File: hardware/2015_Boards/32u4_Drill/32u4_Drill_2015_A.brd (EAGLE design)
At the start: 31.8 x 55.9 mm, 25 parts, among them U2 XBEE-1B3

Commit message: Update some Capacitor Values
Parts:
- C1, C2, C3, C4: value (none) -> 0.01uF
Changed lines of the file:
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@@
 <?xml version="1.0" encoding="utf-8"?>
 <!DOCTYPE eagle SYSTEM "eagle.dtd">
-<eagle version="6.6.0">
+<eagle version="6.5.0">
 <drawing>
 <settings>
@@
 </element>
 <element name="U$4" library="MRDT-2015-General" package="BTM7752G" value="BTM7752G" x="15.875" y="15.5575"/>
-<element name="C1" library="SparkFun-Passives" package="1206" value="" x="11.1125" y="27.94" rot="R90"/>
-<element name="C2" library="SparkFun-Passives" package="1206" value="" x="20.6375" y="27.94" rot="R90"/>
+<element name="C1" library="SparkFun-Passives" package="1206" value="0.01uF" x="11.1125" y="27.94" rot="R90"/>
+<element name="C2" library="SparkFun-Passives" package="1206" value="0.01uF" x="20.6375" y="27.94" rot="R90"/>
 <element name="R2" library="SparkFun-Passives" package="1206" value="4.7k" x="15.875" y="39.37"/>
 <element name="R4" library="SparkFun-Passives" package="1206" value="4.7k" x="15.875" y="37.1475"/>
@@
 <element name="R6" library="SparkFun-Passives" package="1206" value="1k" x="15.875" y="41.5925"/>
 <element name="R7" library="SparkFun-Passives" package="1206" value="" x="15.875" y="43.815"/>
-<element name="C3" library="SparkFun-Passives" package="1206" value="" x="5.08" y="14.605" rot="R180"/>
-<element name="C4" library="SparkFun-Passives" package="1206" value="" x="5.08" y="12.3825" rot="R180"/>
+<element name="C3" library="SparkFun-Passives" package="1206" value="0.01uF" x="5.08" y="14.605" rot="R180"/>
+<element name="C4" library="SparkFun-Passives" package="1206" value="0.01uF" x="5.08" y="12.3825" rot="R180"/>
 </elements>
 <signals>
@@
 <wire x1="14.475" y1="37.1475" x2="14.1575" y2="37.1475" width="0.4064" layer="1"/>
 <wire x1="8.636" y1="34.29" x2="10.16" y2="34.29" width="0.254" layer="16"/>
+<wire x1="13.0175" y1="37.1475" x2="14.1575" y2="37.1475" width="0.254" layer="16"/>
 <wire x1="10.16" y1="34.29" x2="13.0175" y2="37.1475" width="0.254" layer="16"/>
-<wire x1="13.0175" y1="37.1475" x2="14.1575" y2="37.1475" width="0.254" layer="16"/>
 </signal>
 <signal name="INH">

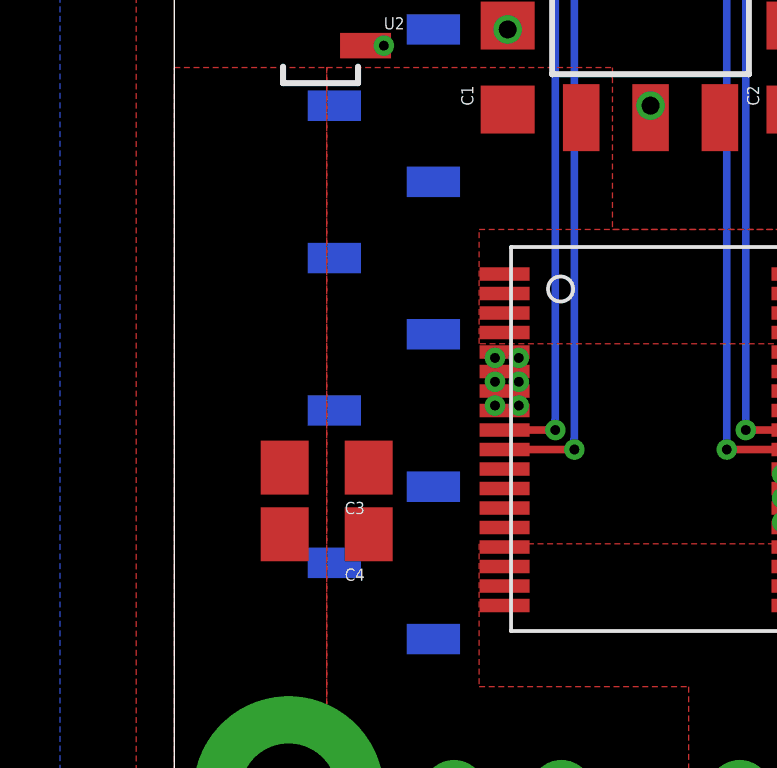
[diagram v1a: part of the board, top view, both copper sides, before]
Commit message: Added a beefy capacitor because the datasheet told me too
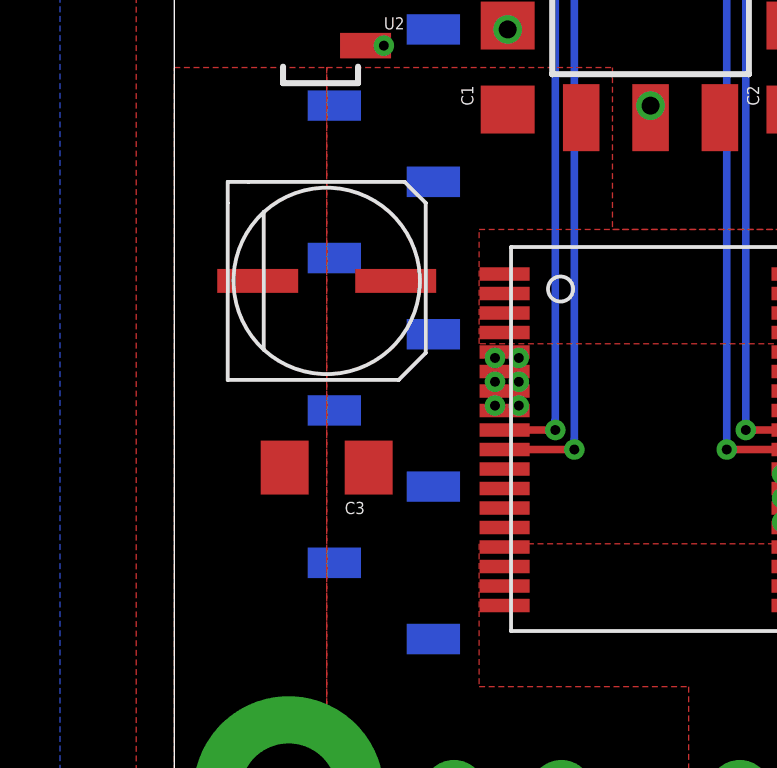
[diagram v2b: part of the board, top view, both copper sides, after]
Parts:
- removed C4: 0.01uF, SparkFun-Passives:1206
- added U$6: 100UF-ELECTRO-CAP, New:ELECTRO-CAP
- C1, C2, C3: value 0.01uF -> 0.1uF
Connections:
- net 12V: now also U$6.POS; no longer C4.1
- net GND: no longer C4.2
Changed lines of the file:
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@@
 <setting verticaltext="up"/>
 </settings>
-<grid distance="0.05" unitdist="inch" unit="inch" style="lines" multiple="1" display="no" altdistance="0.0125" altunitdist="inch" altunit="inch"/>
+<grid distance="0.01" unitdist="inch" unit="inch" style="lines" multiple="1" display="no" altdistance="0.0125" altunitdist="inch" altunit="inch"/>
 <layers>
 <layer number="1" name="Top" color="4" fill="1" visible="yes" active="yes"/>
+<layer number="2" name="Route2" color="1" fill="3" visible="no" active="yes"/>
+<layer number="3" name="Route3" color="4" fill="3" visible="no" active="yes"/>
+<layer number="4" name="Route4" color="1" fill="4" visible="no" active="yes"/>
+<layer number="5" name="Route5" color="4" fill="4" visible="no" active="yes"/>
+<layer number="6" name="Route6" color="1" fill="8" visible="no" active="yes"/>
+<layer number="7" name="Route7" color="4" fill="8" visible="no" active="yes"/>
+<layer number="8" name="Route8" color="1" fill="2" visible="no" active="yes"/>
+<layer number="9" name="Route9" color="4" fill="2" visible="no" active="yes"/>
+<layer number="10" name="Route10" color="1" fill="7" visible="no" active="yes"/>
+<layer number="11" name="Route11" color="4" fill="7" visible="no" active="yes"/>
+<layer number="12" name="Route12" color="1" fill="5" visible="no" active="yes"/>
+<layer number="13" name="Route13" color="4" fill="5" visible="no" active="yes"/>
+<layer number="14" name="Route14" color="1" fill="6" visible="no" active="yes"/>
+<layer number="15" name="Route15" color="4" fill="6" visible="no" active="yes"/>
 <layer number="16" name="Bottom" color="1" fill="1" visible="yes" active="yes"/>
 <layer number="17" name="Pads" color="2" fill="1" visible="yes" active="yes"/>
@@
 </element>
 <element name="U$4" library="MRDT-2015-General" package="BTM7752G" value="BTM7752G" x="15.875" y="15.5575"/>
-<element name="C1" library="SparkFun-Passives" package="1206" value="0.01uF" x="11.1125" y="27.94" rot="R90"/>
-<element name="C2" library="SparkFun-Passives" package="1206" value="0.01uF" x="20.6375" y="27.94" rot="R90"/>
+<element name="C1" library="SparkFun-Passives" package="1206" value="0.1uF" x="11.1125" y="27.94" rot="R90"/>
+<element name="C2" library="SparkFun-Passives" package="1206" value="0.1uF" x="20.6375" y="27.94" rot="R90"/>
 <element name="R2" library="SparkFun-Passives" package="1206" value="4.7k" x="15.875" y="39.37"/>
 <element name="R4" library="SparkFun-Passives" package="1206" value="4.7k" x="15.875" y="37.1475"/>
@@
 <element name="R6" library="SparkFun-Passives" package="1206" value="1k" x="15.875" y="41.5925"/>
 <element name="R7" library="SparkFun-Passives" package="1206" value="" x="15.875" y="43.815"/>
-<element name="C3" library="SparkFun-Passives" package="1206" value="0.01uF" x="5.08" y="14.605" rot="R180"/>
-<element name="C4" library="SparkFun-Passives" package="1206" value="0.01uF" x="5.08" y="12.3825" rot="R180"/>
+<element name="C3" library="SparkFun-Passives" package="1206" value="0.1uF" x="5.08" y="14.605" rot="R180"/>
+<element name="U$6" library="New" package="ELECTRO-CAP" value="100UF-ELECTRO-CAP" x="5.08" y="20.828"/>
 </elements>
 <signals>
@@
 <wire x1="20.6375" y1="29.34" x2="20.6375" y2="29.21" width="0.6096" layer="1"/>
 <contactref element="R6" pad="1"/>
-<contactref element="C4" pad="2"/>
 <contactref element="C3" pad="2"/>
 <polygon width="0.3048" layer="1">
@@
 <contactref element="C1" pad="1"/>
 <contactref element="C3" pad="1"/>
-<contactref element="C4" pad="1"/>
+<contactref element="U$6" pad="POS"/>
 </signal>
 <signal name="TX_0">
@@
 <wire x1="7.9375" y1="43.18" x2="7.9375" y2="46.99" width="0.254" layer="1"/>
 <wire x1="7.9375" y1="46.99" x2="8.255" y2="47.3075" width="0.254" layer="1"/>
-<wire x1="8.255" y1="47.3075" x2="23.1775" y2="47.3075" width="0.254" layer="1"/>
 <wire x1="23.1775" y1="47.3075" x2="23.495" y2="46.99" width="0.254" layer="1"/>
 <wire x1="23.495" y1="46.99" x2="23.495" y2="41.91" width="0.254" layer="1"/>
+<wire x1="8.255" y1="47.3075" x2="23.1775" y2="47.3075" width="0.254" layer="1"/>
 </signal>
 <signal name="RX_0">

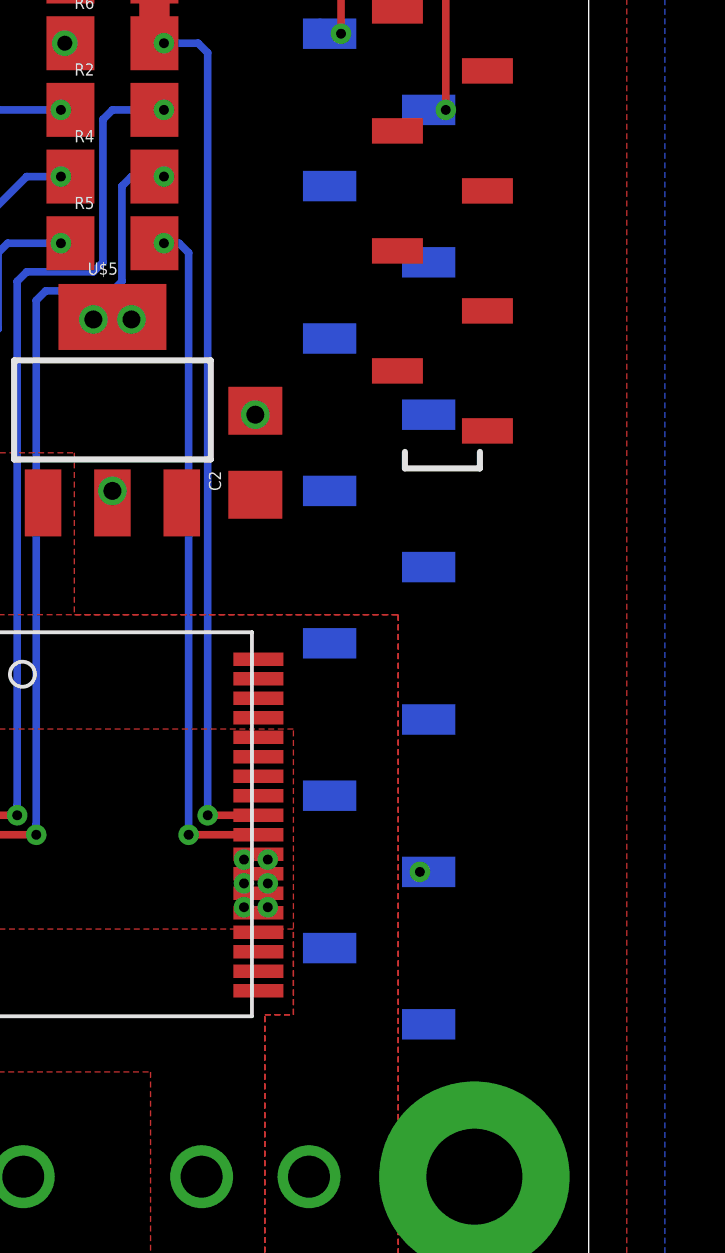
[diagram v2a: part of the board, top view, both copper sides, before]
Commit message: Added sensor breakouts for forgotten sensors
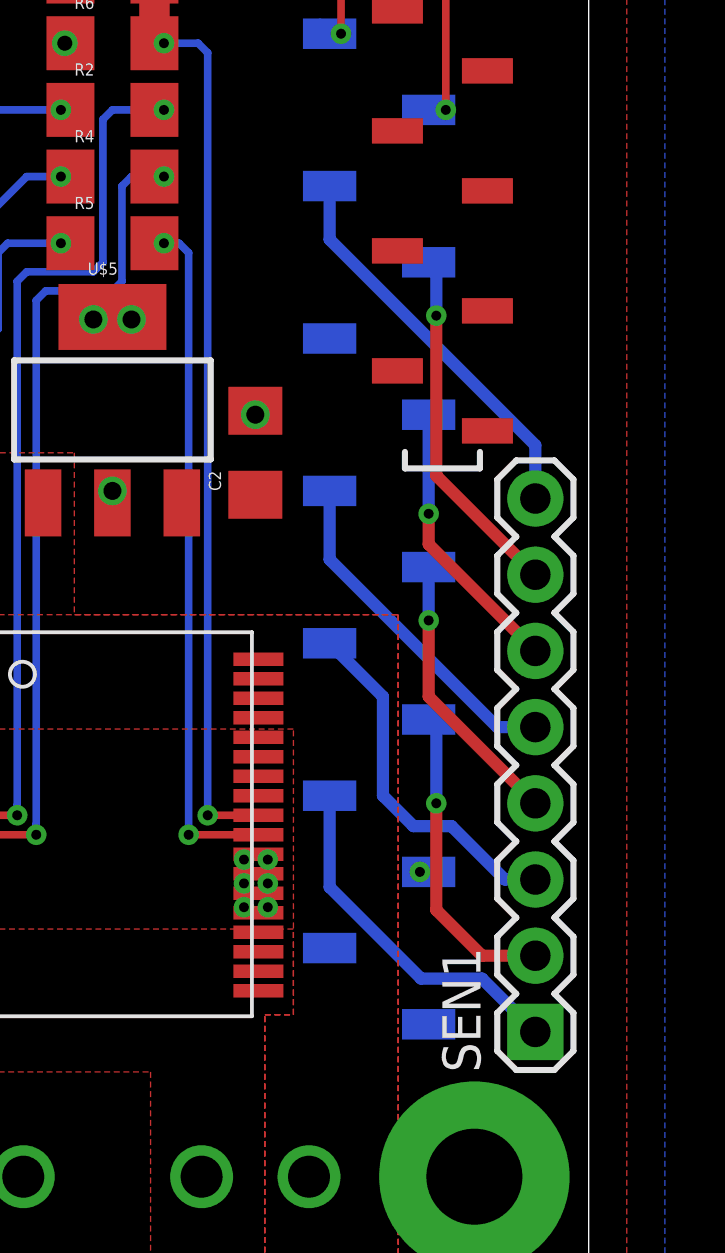
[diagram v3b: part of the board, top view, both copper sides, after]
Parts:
- added SEN1: (no value), SparkFun-Connectors:1X08
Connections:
- new net N$10: SEN1.4, U$1.P$7
- new net N$11: SEN1.5, U$1.P$8
- new net N$12: SEN1.6, U$1.P$9
- new net N$13: SEN1.7, U$1.P$11
- new net N$14: SEN1.8, U$1.P$12
- new net N$7: SEN1.1, U$1.P$4
- new net N$8: SEN1.2, U$1.P$5
- new net N$9: SEN1.3, U$1.P$6
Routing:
- net N$14: track 0.00 -> 13.3 mm
- net N$9: track 0.00 -> 12.4 mm
- net N$7: track 0.00 -> 11.9 mm
- net N$13: track 0.00 -> 11.9 mm, vias 0 -> 1
- net N$11: track 0.00 -> 11.5 mm
- net N$8: track 0.00 -> 10.4 mm, vias 0 -> 1
- net N$12: track 0.00 -> 9.35 mm, vias 0 -> 1
- net N$10: track 0.00 -> 9.35 mm, vias 0 -> 1
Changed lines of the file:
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@@
 <element name="C3" library="SparkFun-Passives" package="1206" value="0.1uF" x="5.08" y="14.605" rot="R180"/>
 <element name="U$6" library="New" package="ELECTRO-CAP" value="100UF-ELECTRO-CAP" x="5.08" y="20.828"/>
+<element name="SEN1" library="SparkFun-Connectors" package="1X08" value="" x="29.972" y="8.636" rot="R90"/>
 </elements>
 <signals>
@@
 <wire x1="14.1575" y1="43.815" x2="14.475" y2="43.815" width="0.4064" layer="1"/>
 </signal>
+<signal name="N$7">
+<contactref element="U$1" pad="P$4"/>
+<contactref element="SEN1" pad="1"/>
+<wire x1="26.162" y1="10.414" x2="23.114" y2="13.462" width="0.4064" layer="16"/>
+<wire x1="23.114" y1="13.462" x2="23.114" y2="16.51" width="0.4064" layer="16"/>
+<wire x1="29.972" y1="8.636" x2="28.194" y2="10.414" width="0.4064" layer="16"/>
+<wire x1="28.194" y1="10.414" x2="26.162" y2="10.414" width="0.4064" layer="16"/>
+</signal>
+<signal name="N$8">
+<contactref element="U$1" pad="P$5"/>
+<contactref element="SEN1" pad="2"/>
+<wire x1="29.972" y1="11.176" x2="28.194" y2="11.176" width="0.4064" layer="1"/>
+<wire x1="28.194" y1="11.176" x2="26.67" y2="12.7" width="0.4064" layer="1"/>
+<wire x1="26.67" y1="12.7" x2="26.67" y2="16.256" width="0.4064" layer="1"/>
+<via x="26.67" y="16.256" extent="1-16" drill="0.3302"/>
+<wire x1="26.67" y1="16.256" x2="26.67" y2="18.796" width="0.4064" layer="16"/>
+<wire x1="26.67" y1="18.796" x2="26.416" y2="19.05" width="0.4064" layer="16"/>
+</signal>
+<signal name="N$9">
+<contactref element="U$1" pad="P$6"/>
+<contactref element="SEN1" pad="3"/>
+<wire x1="29.972" y1="13.716" x2="28.956" y2="13.716" width="0.4064" layer="16"/>
+<wire x1="23.368" y1="21.336" x2="23.114" y2="21.59" width="0.4064" layer="16"/>
+<wire x1="28.956" y1="13.716" x2="27.178" y2="15.494" width="0.4064" layer="16"/>
+<wire x1="27.178" y1="15.494" x2="25.908" y2="15.494" width="0.4064" layer="16"/>
+<wire x1="25.908" y1="15.494" x2="24.892" y2="16.51" width="0.4064" layer="16"/>
+<wire x1="24.892" y1="16.51" x2="24.892" y2="19.812" width="0.4064" layer="16"/>
+<wire x1="24.892" y1="19.812" x2="23.114" y2="21.59" width="0.4064" layer="16"/>
+</signal>
+<signal name="N$10">
+<contactref element="U$1" pad="P$7"/>
+<contactref element="SEN1" pad="4"/>
+<wire x1="29.972" y1="16.256" x2="26.416" y2="19.812" width="0.4064" layer="1"/>
+<wire x1="26.416" y1="19.812" x2="26.416" y2="22.352" width="0.4064" layer="1"/>
+<via x="26.416" y="22.352" extent="1-16" drill="0.3302"/>
+<wire x1="26.416" y1="22.352" x2="26.416" y2="24.13" width="0.4064" layer="16"/>
+</signal>
+<signal name="N$11">
+<contactref element="U$1" pad="P$8"/>
+<contactref element="SEN1" pad="5"/>
+<wire x1="29.972" y1="18.796" x2="28.702" y2="18.796" width="0.4064" layer="16"/>
+<wire x1="28.702" y1="18.796" x2="23.114" y2="24.384" width="0.4064" layer="16"/>
+<wire x1="23.114" y1="24.384" x2="23.114" y2="26.67" width="0.4064" layer="16"/>
+</signal>
+<signal name="N$12">
+<contactref element="U$1" pad="P$9"/>
+<contactref element="SEN1" pad="6"/>
+<wire x1="29.972" y1="21.336" x2="26.416" y2="24.892" width="0.4064" layer="1"/>
+<wire x1="26.416" y1="24.892" x2="26.416" y2="25.908" width="0.4064" layer="1"/>
+<via x="26.416" y="25.908" extent="1-16" drill="0.3302"/>
+<wire x1="26.416" y1="25.908" x2="26.416" y2="29.21" width="0.4064" layer="16"/>
+</signal>
+<signal name="N$13">
+<contactref element="U$1" pad="P$11"/>
+<contactref element="SEN1" pad="7"/>
+<wire x1="29.972" y1="23.876" x2="26.67" y2="27.178" width="0.4064" layer="1"/>
+<wire x1="26.67" y1="27.178" x2="26.67" y2="32.512" width="0.4064" layer="1"/>
+<via x="26.67" y="32.512" extent="1-16" drill="0.3302"/>
+<wire x1="26.67" y1="32.512" x2="26.67" y2="34.036" width="0.4064" layer="16"/>
+<wire x1="26.67" y1="34.036" x2="26.416" y2="34.29" width="0.4064" layer="16"/>
+</signal>
+<signal name="N$14">
+<contactref element="U$1" pad="P$12"/>
+<contactref element="SEN1" pad="8"/>
+<wire x1="29.972" y1="26.416" x2="29.972" y2="28.194" width="0.4064" layer="16"/>
+<wire x1="29.972" y1="28.194" x2="23.114" y2="35.052" width="0.4064" layer="16"/>
+<wire x1="23.114" y1="35.052" x2="23.114" y2="36.83" width="0.4064" layer="16"/>
+</signal>
 </signals>

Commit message: Updated values in Schematic. Makes BOM easier
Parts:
- U$2, U$3: value H_WR-TBL_321*0002VERT -> PLUGABLE SCREW TERMINALS
- U$5: value V_REG_MIC2920 -> 12 TO 3.3 VOLT REG
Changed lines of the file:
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@@
 <element name="R3" library="SparkFun-Passives" package="1206" value="1k" x="15.875" y="47.625" rot="R90"/>
 <element name="U$1" library="MRDT-2015-General" package="32U3_MCU_DIP_SMD" value="32U4_BREAKOU_SMD" x="15.875" y="27.94" rot="MR0"/>
-<element name="U$3" library="MRDT-2015-PowerBoard" package="691321100002" value="H_WR-TBL_321*0002VERT" x="11.1125" y="3.81" rot="MR180">
+<element name="U$3" library="MRDT-2015-PowerBoard" package="691321100002" value="PLUGABLE SCREW TERMINALS" x="11.1125" y="3.81" rot="MR180">
 <attribute name="DIGIKEY_PN" value="732-2763-ND" x="11.1125" y="3.81" size="1.778" layer="28" rot="MR180" display="off"/>
 </element>
-<element name="U$5" library="SparkFun-PowerIC" package="SOT223" value="V_REG_MIC2920" x="15.875" y="29.36875"/>
+<element name="U$5" library="SparkFun-PowerIC" package="SOT223" value="12 TO 3.3 VOLT REG" x="15.875" y="29.36875"/>
 <element name="U2" library="SparkFun" package="XBEE-SMD" value="XBEE-1B3" x="15.875" y="26.67"/>
 <element name="S1" library="SparkFun-Electromechanical" package="STANDOFF-ELECTRICAL" value="STANDOFF_ELECTRICAL" x="3.81" y="52.07"/>
@@
 <element name="S3" library="SparkFun-Electromechanical" package="STANDOFF-ELECTRICAL" value="STANDOFF_ELECTRICAL" x="3.81" y="3.81"/>
 <element name="S4" library="SparkFun-Electromechanical" package="STANDOFF-ELECTRICAL" value="STANDOFF_ELECTRICAL" x="27.94" y="3.81"/>
-<element name="U$2" library="MRDT-2015-PowerBoard" package="691321100002" value="H_WR-TBL_321*0002VERT" x="20.6375" y="3.81" rot="MR180">
+<element name="U$2" library="MRDT-2015-PowerBoard" package="691321100002" value="PLUGABLE SCREW TERMINALS" x="20.6375" y="3.81" rot="MR180">
 <attribute name="DIGIKEY_PN" value="732-2763-ND" x="20.6375" y="3.81" size="1.778" layer="28" rot="MR180" display="off"/>
 </element>
